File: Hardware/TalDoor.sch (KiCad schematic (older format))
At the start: 57 parts, among them J1 SI-52003-F_RJ45, J2 Screw_Terminal_01x02, J3 Conn_01x06_Male, J4 Conn_01x06_Male, P1 Conn_02x18_Odd_Even, P2 Conn_02x18_Odd_Even, Q1 RK7002BM, Q2 RK7002BM, U1 DRV8837, U2 ENC28J60-C/SS, U3 PN532, U4 AG9700, Y1 25MHz

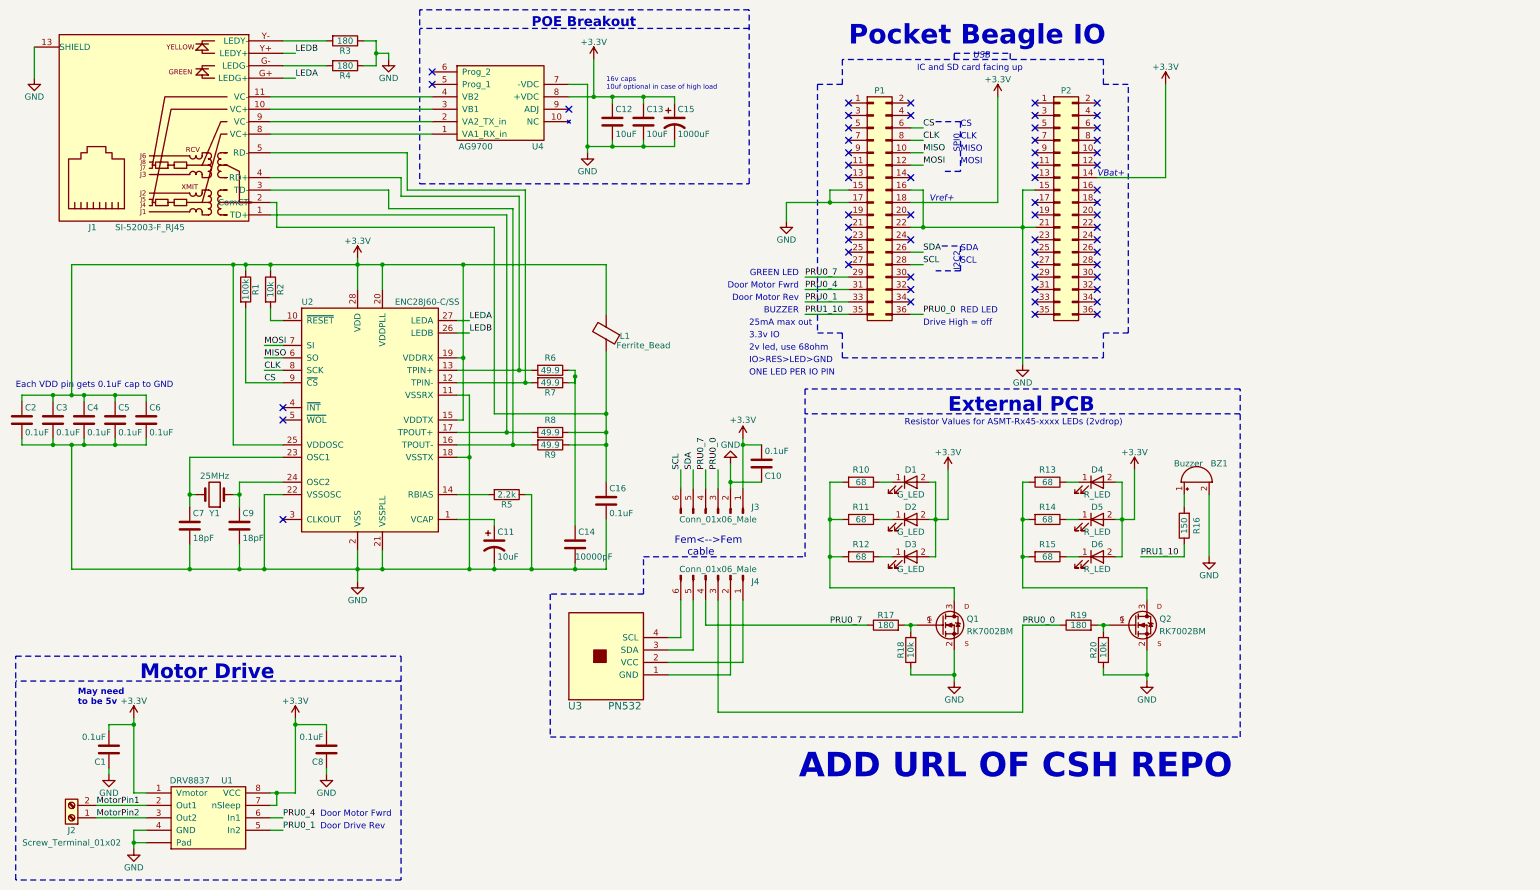
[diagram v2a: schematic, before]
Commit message: Solution to 1 wire LED nitification issue. See LED_NotificationModel.txt
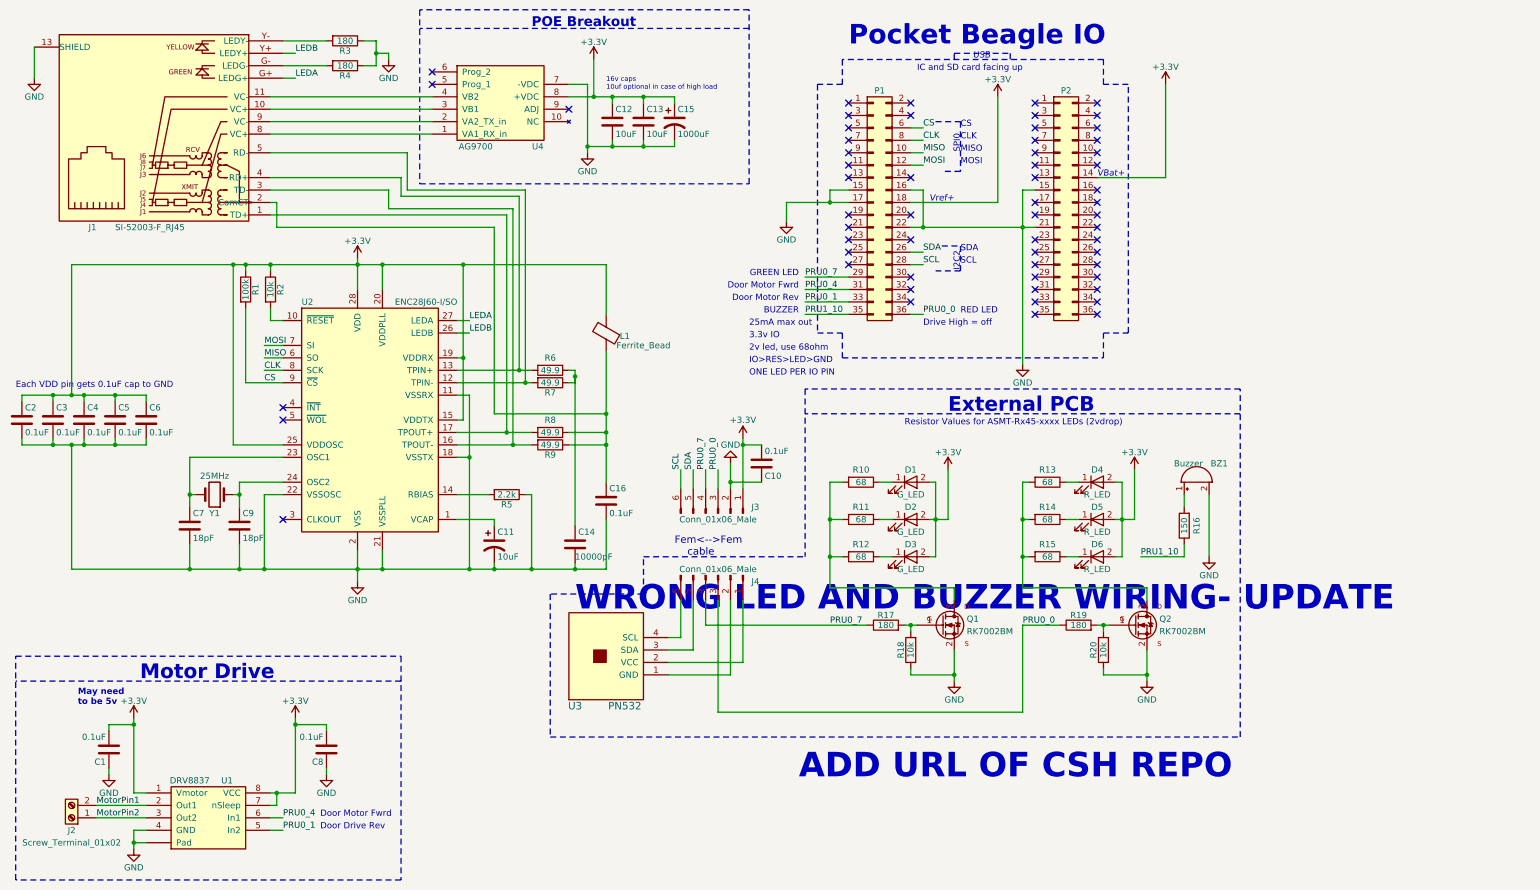
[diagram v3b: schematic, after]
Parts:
- U2: value ENC28J60-C/SS -> ENC28J60-I/SO; footprint Housings_SSOP:SSOP-28_5.3x10.2mm_Pitch0.65mm -> Housings_SOIC:SOIC-28W_7.5x17.9mm_Pitch1.27mm
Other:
- note added: "WRONG LED AND BUZZER WIRING- UPDATE"
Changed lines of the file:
@@
 Rev "1"
 Comp "Spencer Kulbacki - Computer Science House"
-Comment1 "NFC Doorlock hardware with POE support for the Pocket Beagle Devboard"
+Comment1 "NFC Door lock hardware with POE support for the Pocket Beagle Devboard"
 Comment2 ""
 Comment3 ""
@@
 P 3450 4150
 F 0 "U2" H 2900 5100 50  0000 L CNN
-F 1 "ENC28J60-C/SS" H 3650 5100 50  0000 L CNN
-F 2 "Housings_SSOP:SSOP-28_5.3x10.2mm_Pitch0.65mm" H 3450 4150 50  0001 C CIN
+F 1 " ENC28J60-I/SO" H 3650 5100 50  0000 L CNN
+F 2 "Housings_SOIC:SOIC-28W_7.5x17.9mm_Pitch1.27mm" H 3450 4150 50  0001 C CIN
 F 3 "${KIPRJMOD}/Datasheets/3_ENC28J60-H_Ethernet_uC.pdf" H 3450 4150 50  0001 C CNN
 	1    3450 4150
@@
 	750  1150 750  1400
 Wire Wire Line
-	3350 2850 3350 2900
-Wire Wire Line
-	3350 2900 3350 3100
+	3350 2850 3350 3100
 Wire Wire Line
 	4150 3450 4250 3450
@@
 	2450 2900 2450 2950
 Wire Wire Line
-	1050 2900 2350 2900
-Wire Wire Line
-	2350 2900 2450 2900
-Wire Wire Line
-	2450 2900 2650 2900
-Wire Wire Line
-	2650 2900 3350 2900
-Wire Wire Line
-	3350 2900 3550 2900
-Wire Wire Line
-	3550 2900 4200 2900
-Wire Wire Line
-	4200 2900 5350 2900
+	1050 2900 5350 2900
 Wire Wire Line
 	2650 2900 2650 2950
@@
 Connection ~ 2450 2900
 Wire Wire Line
-	1050 5350 2000 5350
-Wire Wire Line
-	2000 5350 2400 5350
-Wire Wire Line
-	2400 5350 2600 5350
-Wire Wire Line
-	2600 5350 3350 5350
-Wire Wire Line
-	3350 5350 3550 5350
-Wire Wire Line
-	3550 5350 4250 5350
-Wire Wire Line
-	4250 5350 4450 5350
-Wire Wire Line
-	4450 5350 4750 5350
-Wire Wire Line
-	4750 5350 5100 5350
-Wire Wire Line
-	5100 5350 5350 5350
+	1050 5350 5350 5350
 Connection ~ 3350 5350
 Wire Wire Line
 	4150 4450 4250 4450
 Wire Wire Line
-	4250 3950 4250 4450
-Wire Wire Line
-	4250 4450 4250 5350
+	4250 3950 4250 5350
 Connection ~ 4250 5350
 Wire Wire Line
@@
 Connection ~ 4450 5350
 Wire Wire Line
-	3350 5200 3350 5350
-Wire Wire Line
-	3350 5350 3350 5450
+	3350 5200 3350 5450
 Wire Wire Line
 	3550 2900 3550 3100
@@
 	4150 3650 4200 3650
 Wire Wire Line
-	4200 2900 4200 3650
-Wire Wire Line
-	4200 3650 4200 4150
+	4200 2900 4200 4150
 Connection ~ 3550 2900
 Wire Wire Line
@@
 	650  4300 650  4350
 Wire Wire Line
-	650  4350 900  4350
-Wire Wire Line
-	900  4350 1050 4350
-Wire Wire Line
-	1050 4350 1150 4350
-Wire Wire Line
-	1150 4350 1400 4350
-Wire Wire Line
-	1400 4350 1650 4350
+	650  4350 1650 4350
 Wire Wire Line
 	1400 4350 1400 4300
@@
 	650  4000 650  3950
 Wire Wire Line
-	650  3950 900  3950
-Wire Wire Line
-	900  3950 1050 3950
-Wire Wire Line
-	1050 3950 1150 3950
-Wire Wire Line
-	1150 3950 1400 3950
-Wire Wire Line
-	1400 3950 1650 3950
+	650  3950 1650 3950
 Wire Wire Line
 	1400 3950 1400 4000
@@
 	2350 4750 2400 4750
 Wire Wire Line
-	2400 4650 2400 4750
-Wire Wire Line
-	2400 4750 2400 4850
+	2400 4650 2400 4850
 Connection ~ 2400 4750
 Wire Wire Line
@@
 	2750 4450 2000 4450
 Wire Wire Line
-	2000 4450 2000 4750
-Wire Wire Line
-	2000 4750 2000 4850
+	2000 4450 2000 4850
 Wire Wire Line
 	2050 4750 2000 4750
@@
 	4700 2300 4700 3850
 Wire Wire Line
-	4150 3850 4700 3850
-Wire Wire Line
-	4700 3850 4750 3850
-Wire Wire Line
-	4150 3750 4650 3750
-Wire Wire Line
-	4650 3750 4750 3750
+	4150 3850 4750 3850
+Wire Wire Line
+	4150 3750 4750 3750
 Wire Wire Line
 	4650 3750 4650 2350
@@
 	4600 2450 4600 4350
 Wire Wire Line
-	4150 4350 4600 4350
-Wire Wire Line
-	4600 4350 4750 4350
-Wire Wire Line
-	4150 4250 4550 4250
-Wire Wire Line
-	4550 4250 4750 4250
+	4150 4350 4750 4350
+Wire Wire Line
+	4150 4250 4750 4250
 Wire Wire Line
 	4550 2500 4550 4250
@@
 	3600 1250 3600 1200
 Wire Wire Line
-	3500 1100 3500 1200
-Wire Wire Line
-	3500 1200 3500 1300
+	3500 1100 3500 1300
 Wire Wire Line
 	3600 1200 3500 1200
@@
 	5350 4250 5050 4250
 Wire Wire Line
-	5350 3600 5350 4100
-Wire Wire Line
-	5350 4100 5350 4250
-Wire Wire Line
-	5350 4250 5350 4350
-Wire Wire Line
-	5350 4350 5350 4650
+	5350 3600 5350 4650
 Wire Wire Line
 	5350 4350 5050 4350
@@
 	5050 3750 5100 3750
 Wire Wire Line
-	5100 3750 5100 3800
-Wire Wire Line
-	5100 3800 5100 3850
+	5100 3750 5100 3850
 Wire Wire Line
 	5100 3850 5050 3850
@@
 	7150 2300 7150 2400
 Wire Wire Line
-	6800 2400 7150 2400
-Wire Wire Line
-	7150 2400 7300 2400
-Wire Wire Line
-	7800 2600 7900 2600
-Wire Wire Line
-	7900 2600 8700 2600
-Wire Wire Line
-	8700 2600 8800 2600
+	6800 2400 7300 2400
+Wire Wire Line
+	7800 2600 8800 2600
 Wire Wire Line
 	7900 2600 7900 2300
@@
 	10450 4100 6950 4100
 Wire Wire Line
-	2850 7150 2850 6600
-Wire Wire Line
-	2850 6600 2850 6550
-Wire Wire Line
-	2650 7150 2700 7150
-Wire Wire Line
-	2700 7150 2850 7150
+	2850 7150 2850 6550
+Wire Wire Line
+	2650 7150 2850 7150
 Wire Wire Line
 	1550 7150 1650 7150
 Wire Wire Line
-	1550 6550 1550 6600
-Wire Wire Line
-	1550 6600 1550 7150
-Wire Wire Line
-	1550 7450 1550 7550
-Wire Wire Line
-	1550 7550 1550 7600
+	1550 6550 1550 7150
+Wire Wire Line
+	1550 7450 1550 7600
 Wire Wire Line
 	1650 7550 1550 7550
@@
 	5050 1450 5200 1450
 Wire Wire Line
-	5200 1450 5200 1950
-Wire Wire Line
-	5200 1950 5200 2000
+	5200 1450 5200 2000
 Wire Wire Line
 	5900 1550 5900 1600
@@
 	5400 1900 5400 1950
 Wire Wire Line
-	5200 1950 5400 1950
-Wire Wire Line
-	5400 1950 5650 1950
-Wire Wire Line
-	5650 1950 5900 1950
+	5200 1950 5900 1950
 Connection ~ 5200 1950
 Wire Wire Line
@@
 	1650 7450 1550 7450
 Wire Wire Line
-	5050 1550 5250 1550
-Wire Wire Line
-	5250 1550 5400 1550
-Wire Wire Line
-	5400 1550 5650 1550
-Wire Wire Line
-	5650 1550 5900 1550
+	5050 1550 5900 1550
 Wire Wire Line
 	7950 4650 8000 4650
 Wire Wire Line
-	8000 4650 8000 4950
-Wire Wire Line
-	8000 4950 8000 5250
+	8000 4650 8000 5250
 Wire Wire Line
 	8000 5250 7950 5250
@@
 	8750 4650 8700 4650
 Wire Wire Line
-	8700 4650 8700 4950
-Wire Wire Line
-	8700 4950 8700 5250
-Wire Wire Line
-	8700 5250 8700 5500
+	8700 4650 8700 5500
 Wire Wire Line
 	8700 5250 8750 5250
@@
 	7800 3300 7900 3300
 Wire Wire Line
-	8700 2300 8700 2600
-Wire Wire Line
-	8700 2600 8700 3700
+	8700 2300 8700 3700
 Connection ~ 8700 2600
 Wire Wire Line
 	7300 3000 6950 3000
 Wire Wire Line
-	7950 4950 8000 4950
-Wire Wire Line
-	8000 4950 8100 4950
+	7950 4950 8100 4950
 Wire Wire Line
 	8700 4950 8750 4950
@@
 	9450 4650 9500 4650
 Wire Wire Line
-	9500 4650 9500 4950
-Wire Wire Line
-	9500 4950 9500 5250
+	9500 4650 9500 5250
 Wire Wire Line
 	9500 5250 9450 5250
 Wire Wire Line
-	9450 4950 9500 4950
-Wire Wire Line
-	9500 4950 9600 4950
+	9450 4950 9600 4950
 Connection ~ 9500 4950
 Wire Wire Line
@@
 Connection ~ 8700 5250
 Wire Wire Line
-	9700 6000 9700 6200
-Wire Wire Line
-	9700 6200 9700 6250
-Wire Wire Line
-	9300 5800 9350 5800
-Wire Wire Line
-	9350 5800 9400 5800
+	9700 6000 9700 6250
+Wire Wire Line
+	9300 5800 9400 5800
 Wire Wire Line
 	9350 5800 9350 5850
@@
 	8150 5600 8150 5500
 Wire Wire Line
-	8150 6000 8150 6200
-Wire Wire Line
-	8150 6200 8150 6250
-Wire Wire Line
-	7750 5800 7800 5800
-Wire Wire Line
-	7800 5800 7850 5800
+	8150 6000 8150 6250
+Wire Wire Line
+	7750 5800 7850 5800
 Wire Wire Line
 	7800 5800 7800 5850
@@
 	6150 5800 7450 5800
 Wire Wire Line
-	7150 5500 8150 5500
-Wire Wire Line
-	7150 4650 7150 4950
-Wire Wire Line
-	7150 4950 7150 5250
-Wire Wire Line
-	7150 5250 7150 5500
+	8150 5500 7150 5500
+Wire Wire Line
+	7150 5500 7150 4650
 $Comp
 L Conn_01x06_Male J4
@@
 $EndComp
 Wire Wire Line
-	6350 4500 6350 4650
-Wire Wire Line
-	6350 4650 6350 4700
-Wire Wire Line
-	6450 4300 6450 4350
-Wire Wire Line
-	6450 4350 6450 4700
+	6350 4500 6350 4700
+Wire Wire Line
+	6450 4300 6450 4700
 Wire Wire Line
 	5850 5900 5950 5900
@@
 Wire Notes Line
 	5650 5250 6950 5250
+Text Notes 5100 5700 0    197  ~ 39
+WRONG LED AND BUZZER WIRING- UPDATE
 $EndSCHEMATC

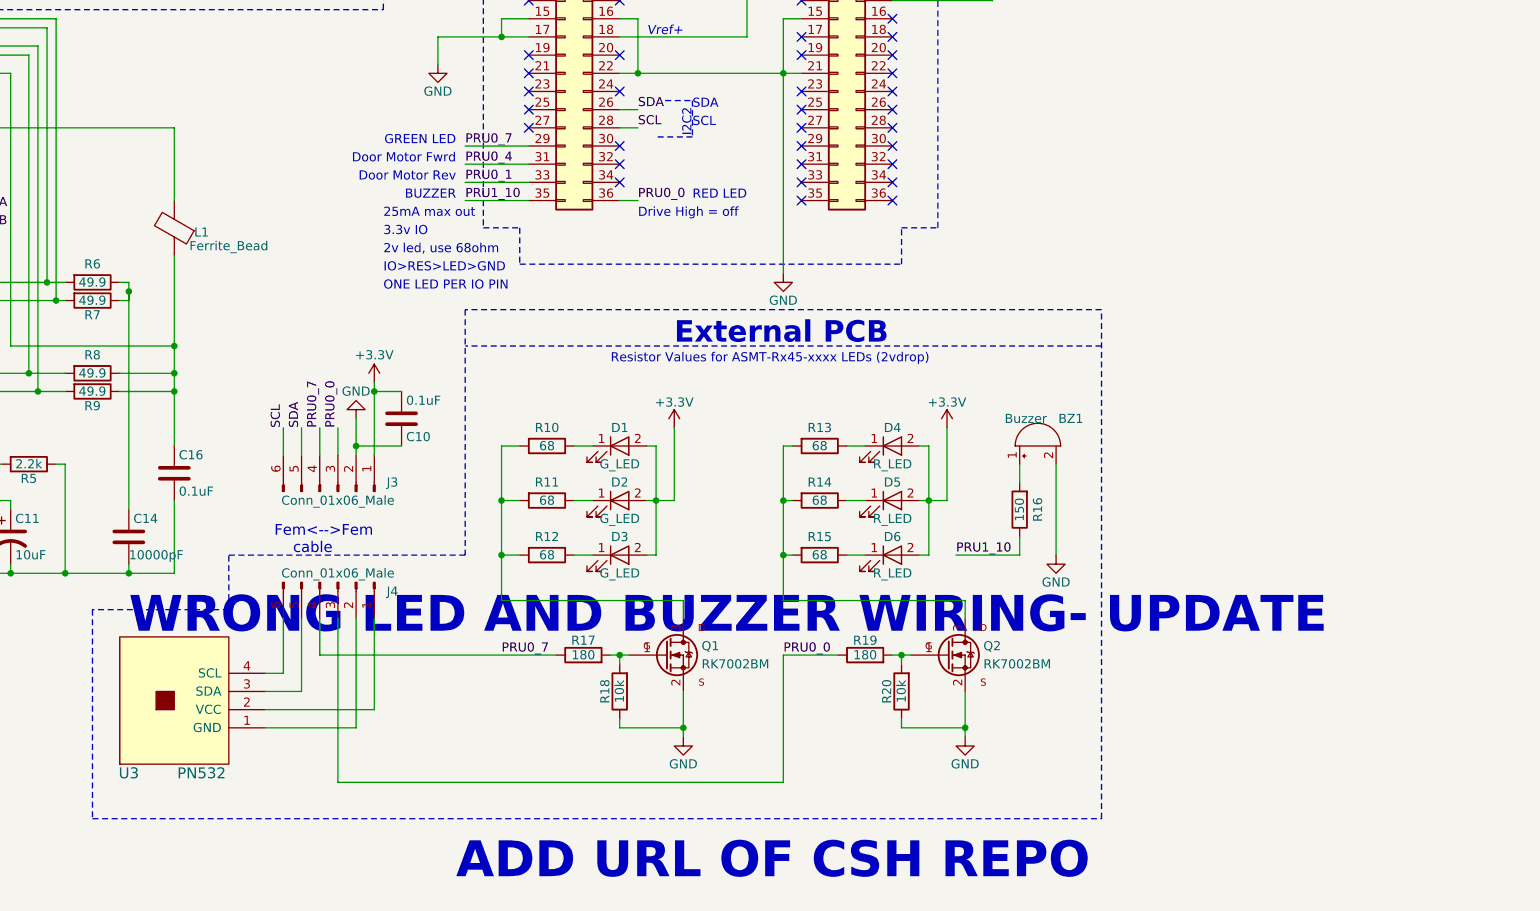
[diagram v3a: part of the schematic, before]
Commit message: Updated schematic with N/Pmos LED format for single IO drive. Updated BOM
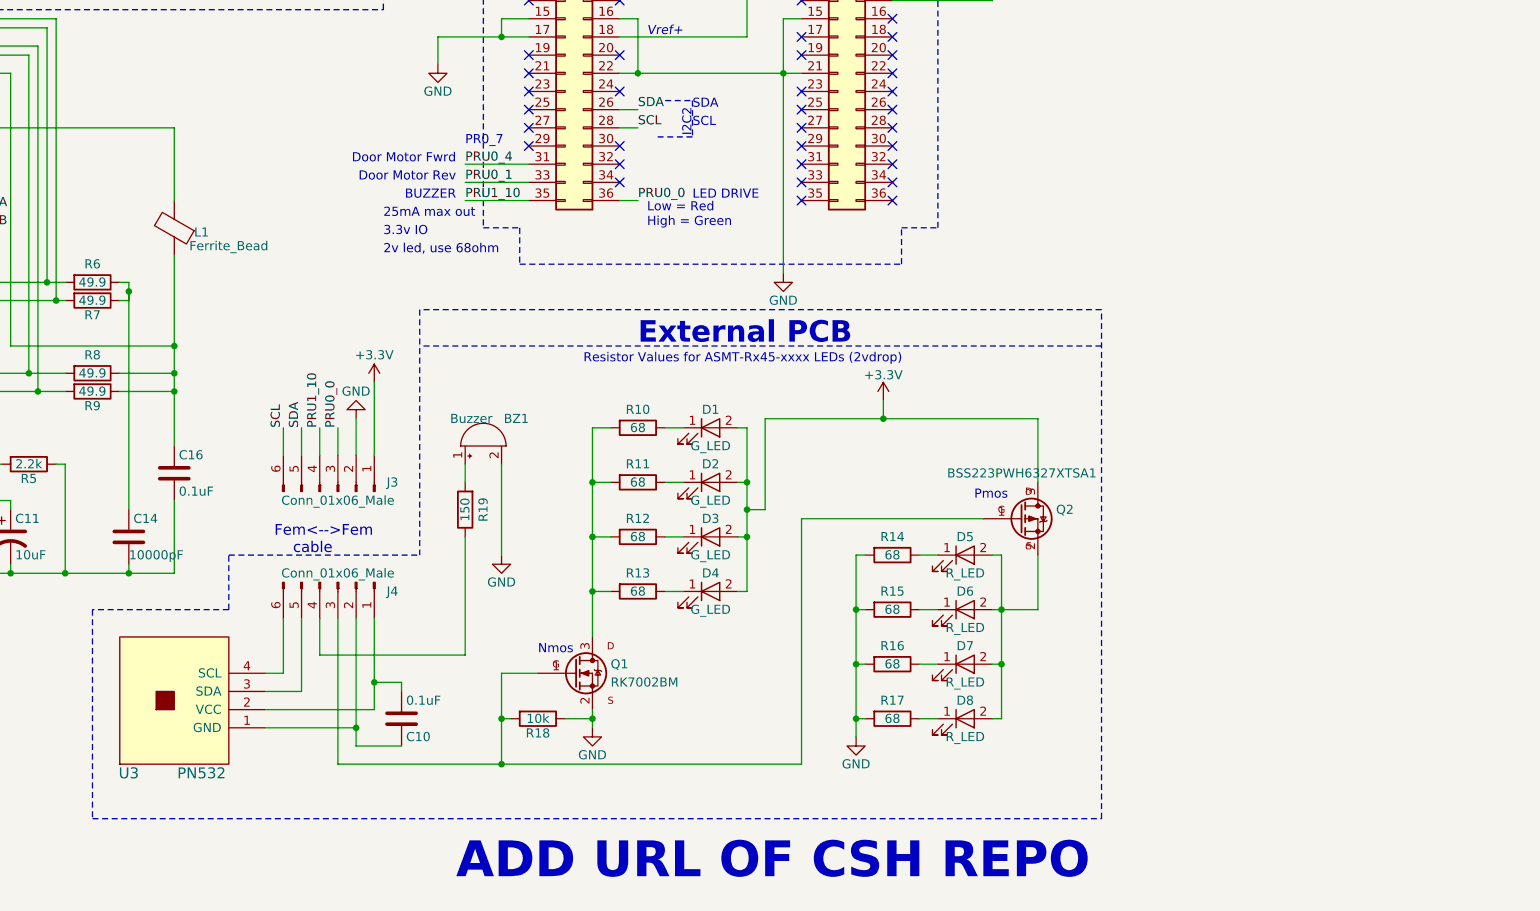
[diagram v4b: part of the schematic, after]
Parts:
- removed Q2: RK7002BM, TO_SOT_Packages_SMD:SOT-23, symbol RK7002BM
- removed R19: 180, Resistors_SMD:R_0603, symbol R
- removed R20: 10k, Resistors_SMD:R_0603, symbol R
- added D4: G_LED, LEDs:LED_0603, symbol LED
- added D8: R_LED, LEDs:LED_0603, symbol LED
- added Q2: BSS223PWH6327XTSA1, TO_SOT_Packages_SMD:SOT-323_SC-70, symbol BSS223PWH6327XTSA1
- added R13: 68, Resistors_SMD:R_0603, symbol R
- R17: value 180 -> 68
- renumbered D4 to D5, D5 to D6, D6 to D7, R13 to R14, R14 to R15, R15 to R16, R16 to R19
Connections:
- net +3V3: now also D4.2 (A), Q2.3 (D); no longer C10.2, D5.2 (A), D6.2 (A), D7.2 (A)
- net GND: now also R14.2, R15.2, R16.2, R17.2; no longer C10.1
- net PRU0_0: no longer J4.3 (Pin_3)
- net PRU1_10: now also J3.4 (Pin_4); no longer R19.1
- net at J4.2 (Pin_2), U3.1 (GND): now also C10.1
- net at J4.1 (Pin_1), U3.2 (VCC): now also C10.2
- net at Q1.3 (D), R10.2, R11.2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: now also R13.2
- net at Q1.1 (G), R18.2: now also J4.3 (Pin_3), Q2.1 (G); no longer R17.2
- removed net PRU0_7: J3.4 (Pin_4), J4.4 (Pin_4), P1.29 (Pin_29), R17.1
- new net: D5.2 (A), D6.2 (A), D7.2 (A), D8.2 (A), Q2.2 (S)
- new net: J4.4 (Pin_4), R19.1
- new net: D4.1 (K), R13.1
- new net: D8.1 (K), R17.1
- no-connect marks 59 -> 60
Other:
- note added: "LED DRIVE"
- note added: "Low = Red\nHigh = Green"
- note added: "Nmos"
- note added: "PR0_7"
- note added: "Pmos"
- note removed: "Drive High = off"
- note removed: "GREEN LED"
- note removed: "IO>RES>LED>GND"
- note removed: "ONE LED PER IO PIN"
- note removed: "RED LED"
- note removed: "WRONG LED AND BUZZER WIRING- UPDATE"
- moved on the sheet: BZ1, C10, D1, D2, D3, D5, D6, D7, Q1, R10, R11, R12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
